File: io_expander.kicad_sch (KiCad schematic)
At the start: 4 parts, among them J701 Conn_01x08, J702 Conn_01x08, U701 PCA9535PW

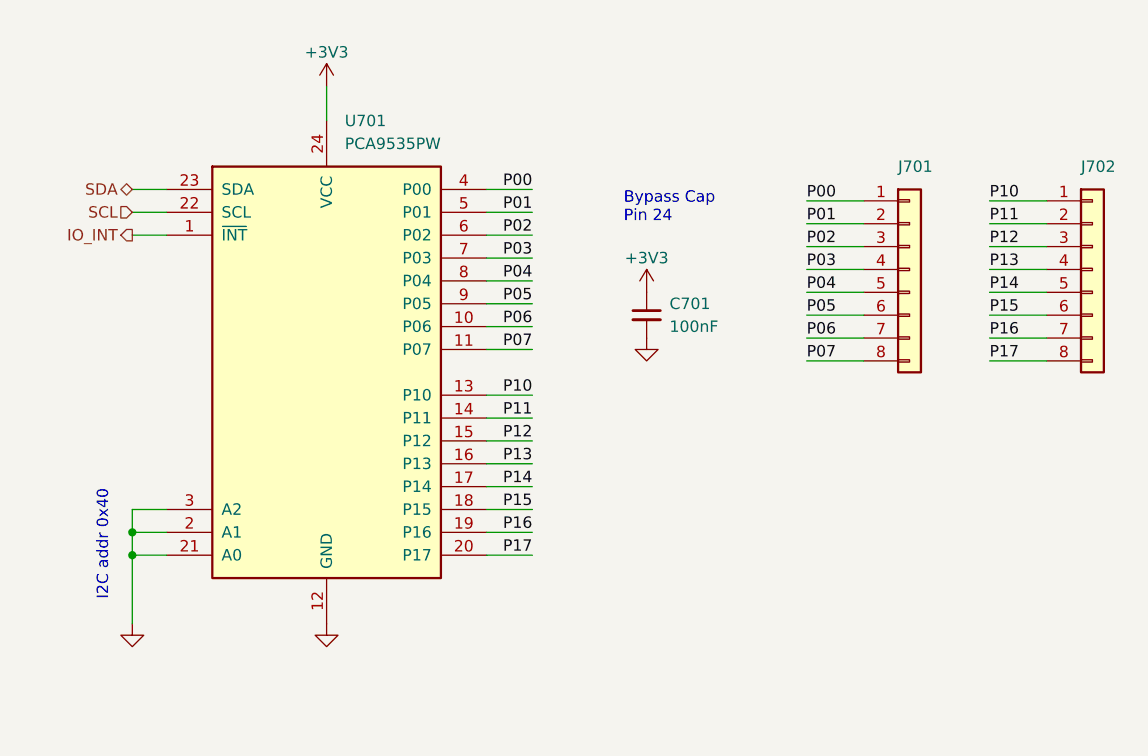
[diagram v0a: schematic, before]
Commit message: add RTC, humidity and temp sensors
updated footprint paths
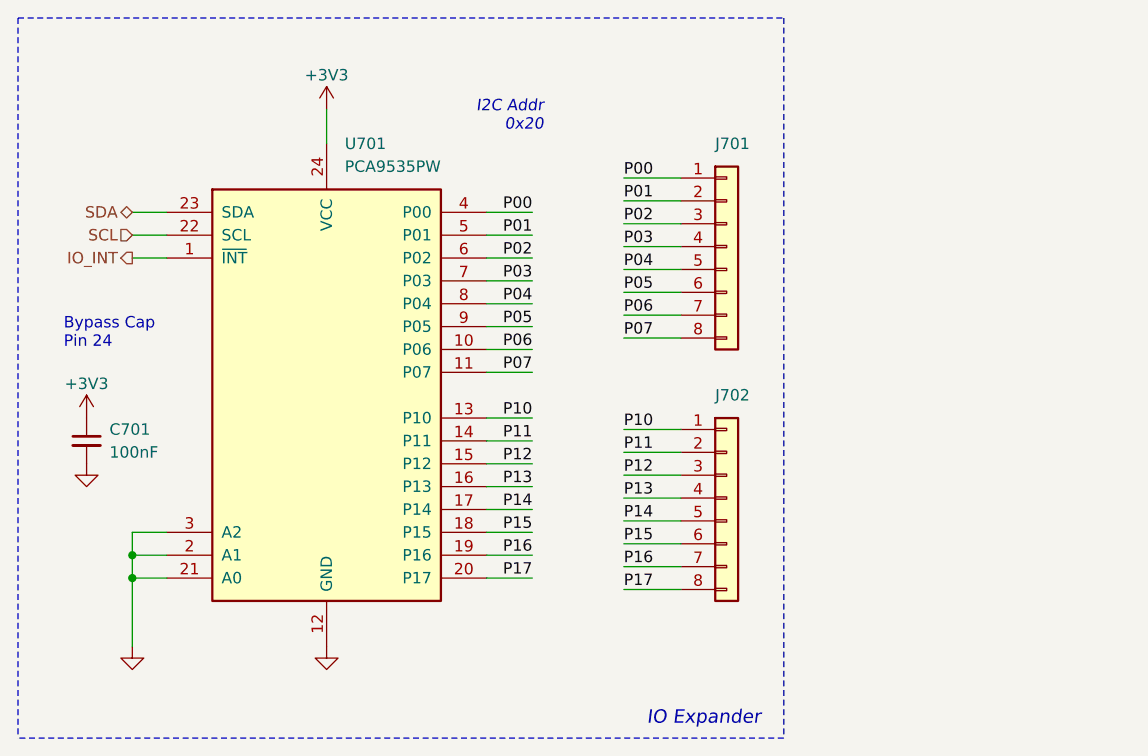
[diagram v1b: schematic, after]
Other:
- note added: "I2C Addr 0x20"
- note added: "IO Expander"
- note removed: "I2C addr 0x40"
- moved on the sheet: C701, J701, J702, U701

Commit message: revise schematics
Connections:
- net P00: now also J701.8 (Pin_8); no longer J701.1 (Pin_1)
- net P01: now also J701.7 (Pin_7); no longer J701.2 (Pin_2)
- net P02: now also J701.6 (Pin_6); no longer J701.3 (Pin_3)
- net P03: now also J701.5 (Pin_5); no longer J701.4 (Pin_4)
- net P04: now also J701.4 (Pin_4); no longer J701.5 (Pin_5)
- net P05: now also J701.3 (Pin_3); no longer J701.6 (Pin_6)
- net P06: now also J701.2 (Pin_2); no longer J701.7 (Pin_7)
- net P07: now also J701.1 (Pin_1); no longer J701.8 (Pin_8)
- net P10: now also J702.8 (Pin_8); no longer J702.1 (Pin_1)
- net P11: now also J702.7 (Pin_7); no longer J702.2 (Pin_2)
- net P12: now also J702.6 (Pin_6); no longer J702.3 (Pin_3)
- net P13: now also J702.5 (Pin_5); no longer J702.4 (Pin_4)
- net P14: now also J702.4 (Pin_4); no longer J702.5 (Pin_5)
- net P15: now also J702.3 (Pin_3); no longer J702.6 (Pin_6)
- net P16: now also J702.2 (Pin_2); no longer J702.7 (Pin_7)
- net P17: now also J702.1 (Pin_1); no longer J702.8 (Pin_8)
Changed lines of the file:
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@@
     (effects (font (size 1.27 1.27)) (justify right bottom))
   )
-  (label "P06" (at 82.55 48.26 0) (fields_autoplaced)
+  (label "P06" (at 82.55 35.56 0) (fields_autoplaced)
     (effects (font (size 1.27 1.27)) (justify left bottom))
   )
@@
     (effects (font (size 1.27 1.27)) (justify right bottom))
   )
-  (label "P00" (at 82.55 33.02 0) (fields_autoplaced)
+  (label "P00" (at 82.55 50.8 0) (fields_autoplaced)
     (effects (font (size 1.27 1.27)) (justify left bottom))
   )
-  (label "P16" (at 82.55 76.2 0) (fields_autoplaced)
+  (label "P16" (at 82.55 63.5 0) (fields_autoplaced)
     (effects (font (size 1.27 1.27)) (justify left bottom))
   )
-  (label "P12" (at 82.55 66.04 0) (fields_autoplaced)
+  (label "P12" (at 82.55 73.66 0) (fields_autoplaced)
     (effects (font (size 1.27 1.27)) (justify left bottom))
   )
-  (label "P13" (at 82.55 68.58 0) (fields_autoplaced)
+  (label "P13" (at 82.55 71.12 0) (fields_autoplaced)
     (effects (font (size 1.27 1.27)) (justify left bottom))
   )
-  (label "P04" (at 82.55 43.18 0) (fields_autoplaced)
+  (label "P04" (at 82.55 40.64 0) (fields_autoplaced)
     (effects (font (size 1.27 1.27)) (justify left bottom))
   )
@@
     (effects (font (size 1.27 1.27)) (justify right bottom))
   )
-  (label "P15" (at 82.55 73.66 0) (fields_autoplaced)
+  (label "P15" (at 82.55 66.04 0) (fields_autoplaced)
     (effects (font (size 1.27 1.27)) (justify left bottom))
   )
@@
     (effects (font (size 1.27 1.27)) (justify right bottom))
   )
-  (label "P01" (at 82.55 35.56 0) (fields_autoplaced)
+  (label "P01" (at 82.55 48.26 0) (fields_autoplaced)
     (effects (font (size 1.27 1.27)) (justify left bottom))
   )
@@
     (effects (font (size 1.27 1.27)) (justify right bottom))
   )
-  (label "P03" (at 82.55 40.64 0) (fields_autoplaced)
+  (label "P03" (at 82.55 43.18 0) (fields_autoplaced)
     (effects (font (size 1.27 1.27)) (justify left bottom))
   )
@@
     (effects (font (size 1.27 1.27)) (justify right bottom))
   )
-  (label "P07" (at 82.55 50.8 0) (fields_autoplaced)
+  (label "P07" (at 82.55 33.02 0) (fields_autoplaced)
     (effects (font (size 1.27 1.27)) (justify left bottom))
   )
-  (label "P14" (at 82.55 71.12 0) (fields_autoplaced)
+  (label "P14" (at 82.55 68.58 0) (fields_autoplaced)
     (effects (font (size 1.27 1.27)) (justify left bottom))
   )
@@
     (effects (font (size 1.27 1.27)) (justify right bottom))
   )
-  (label "P17" (at 82.55 78.74 0) (fields_autoplaced)
+  (label "P17" (at 82.55 60.96 0) (fields_autoplaced)
     (effects (font (size 1.27 1.27)) (justify left bottom))
   )
-  (label "P11" (at 82.55 63.5 0) (fields_autoplaced)
+  (label "P11" (at 82.55 76.2 0) (fields_autoplaced)
     (effects (font (size 1.27 1.27)) (justify left bottom))
   )
-  (label "P05" (at 82.55 45.72 0) (fields_autoplaced)
+  (label "P05" (at 82.55 38.1 0) (fields_autoplaced)
     (effects (font (size 1.27 1.27)) (justify left bottom))
   )
-  (label "P02" (at 82.55 38.1 0) (fields_autoplaced)
+  (label "P02" (at 82.55 45.72 0) (fields_autoplaced)
     (effects (font (size 1.27 1.27)) (justify left bottom))
   )
@@
     (effects (font (size 1.27 1.27)) (justify right bottom))
   )
-  (label "P10" (at 82.55 60.96 0) (fields_autoplaced)
+  (label "P10" (at 82.55 78.74 0) (fields_autoplaced)
     (effects (font (size 1.27 1.27)) (justify left bottom))
   )
